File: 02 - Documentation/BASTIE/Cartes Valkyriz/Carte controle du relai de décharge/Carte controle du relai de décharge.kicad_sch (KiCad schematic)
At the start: 8 parts, among them K1 SSR CPC1394GR

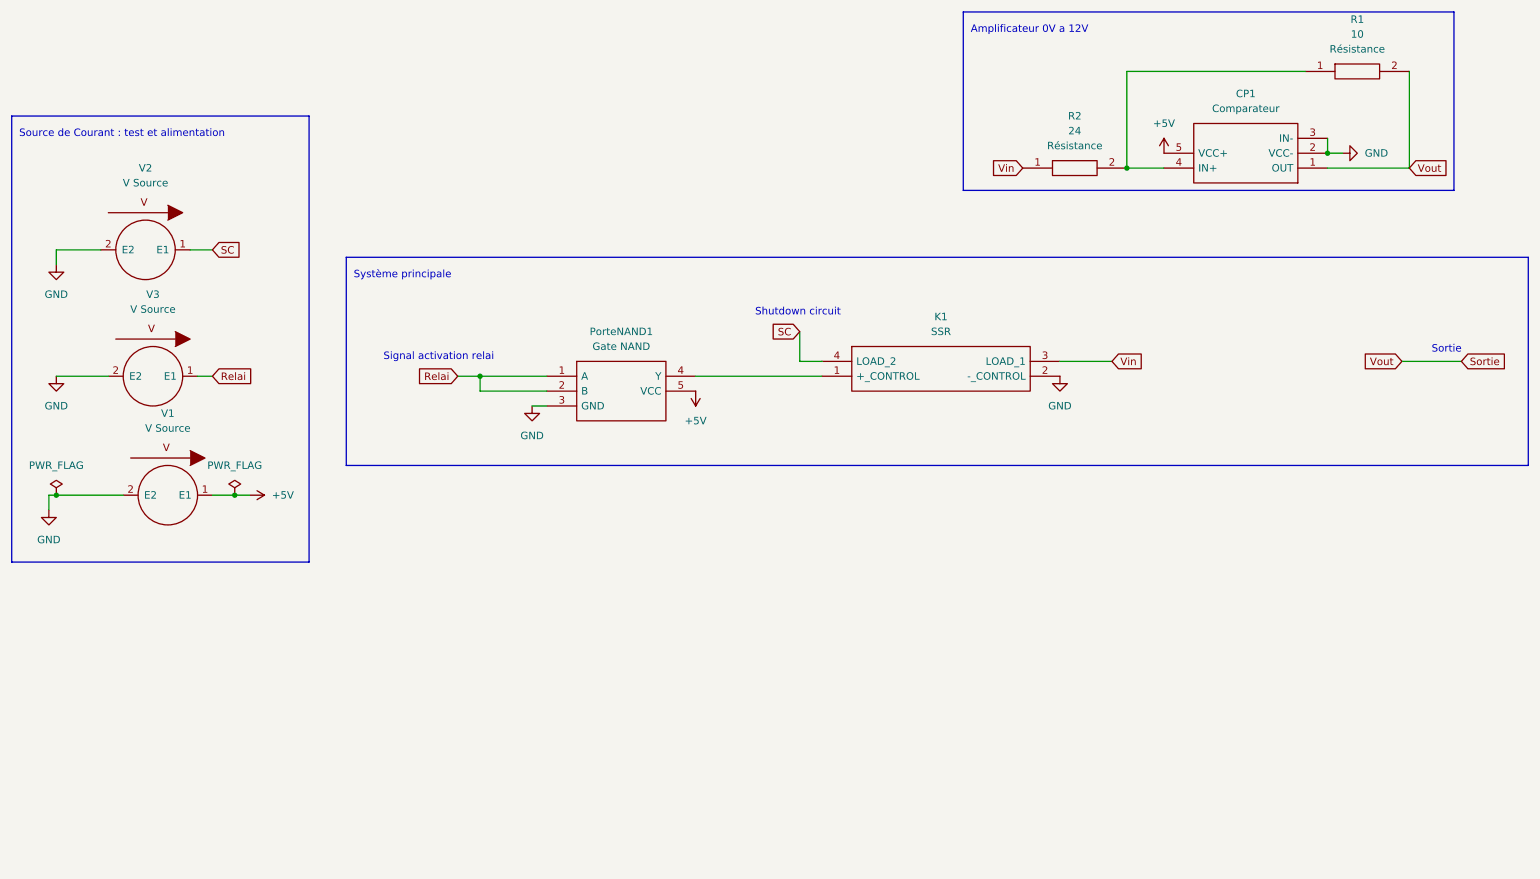
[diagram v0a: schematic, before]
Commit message: Modif carte controle relai décharge
mis a jour des pinns et de l'alimentation.
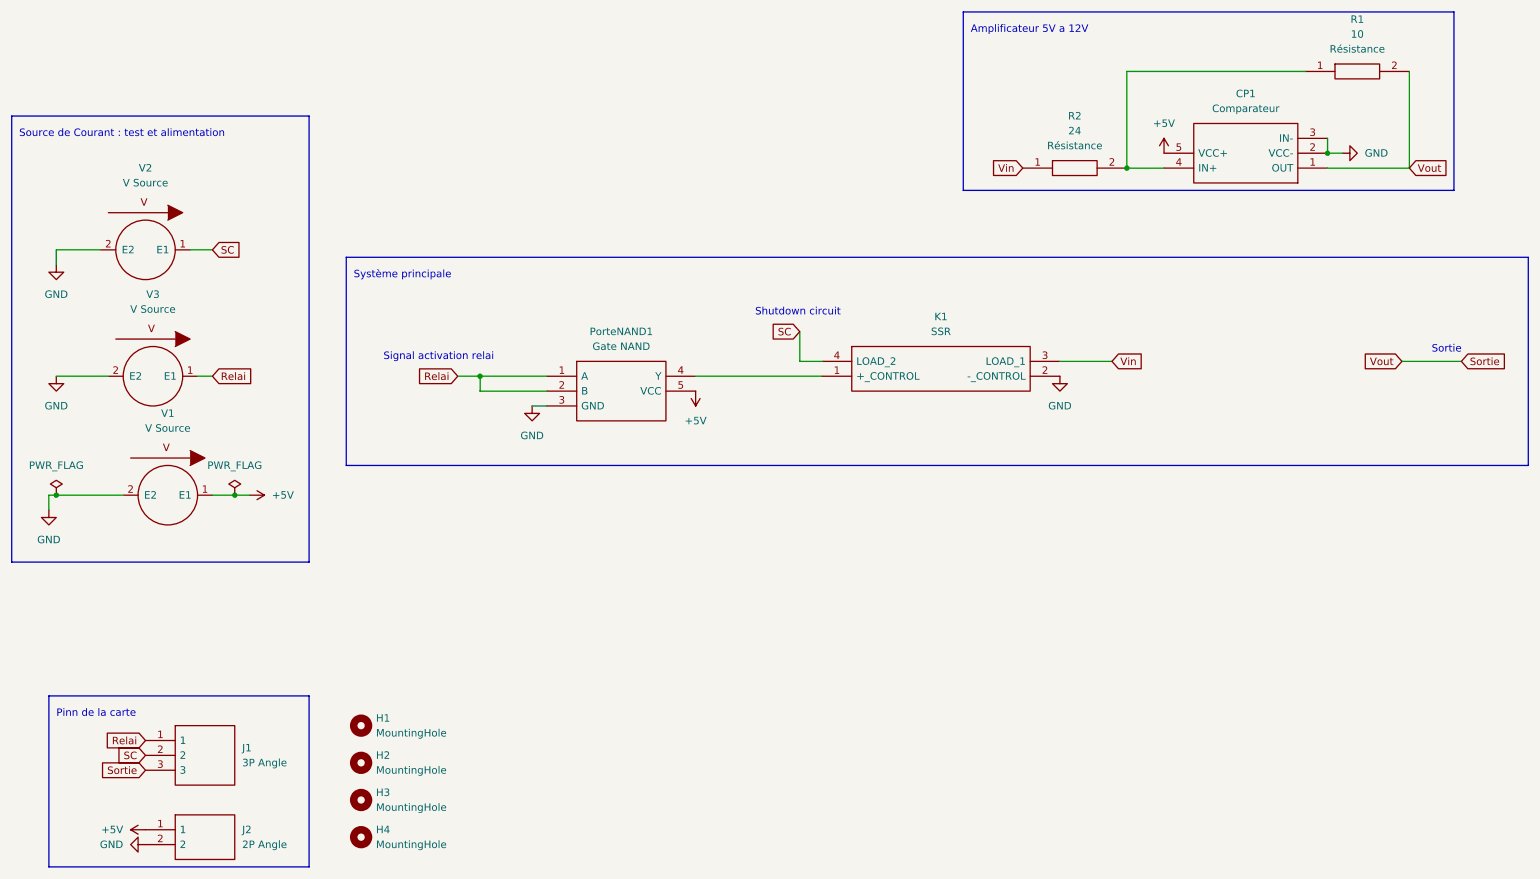
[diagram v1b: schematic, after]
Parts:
- added H1, H2, H3, H4: MountingHole, symbol Mechanical:MountingHole
- added J1: 3P Angle 22-12-2034, EPSA_lib:22122034, symbol EPSA_lib:3P Angle 22-12-2034
- added J2: 2P Angle 171857-4002, EPSA_lib:1718574002, symbol EPSA_lib:2P Angle 171857-4002
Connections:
- net +5V: now also J2.1
- net GND: now also J2.2
- net Relai: now also J1.1
- net SC: now also J1.2
- net Sortie: now also J1.3
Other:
- note added: "Amplificateur 5V a 12V"
- note added: "Pinn de la carte"
- note removed: "Amplificateur 0V a 12V"
